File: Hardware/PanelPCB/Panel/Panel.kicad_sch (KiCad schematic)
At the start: 13 parts, among them J1 RJ45, J2 Conn_01x03_Socket, U1 AP2204R-5.0, U2 SN74LV1T34DBV

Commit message: Export schematics
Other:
- company: (none) -> M. Scholjegerdes
- title: (none) -> BugWiper 2.0 Control Panel PCB
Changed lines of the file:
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@@
 (kicad_sch (version 20230121) (generator eeschema)
   (paper "A4")
+  (title_block
+    (title "BugWiper 2.0 Control Panel PCB")
+    (date "2025-01-27")
+    (company "M. Scholjegerdes")
+  )
   (junction (at 180.34 48.26) (diameter 0) (color 0 0 0 0)
   )

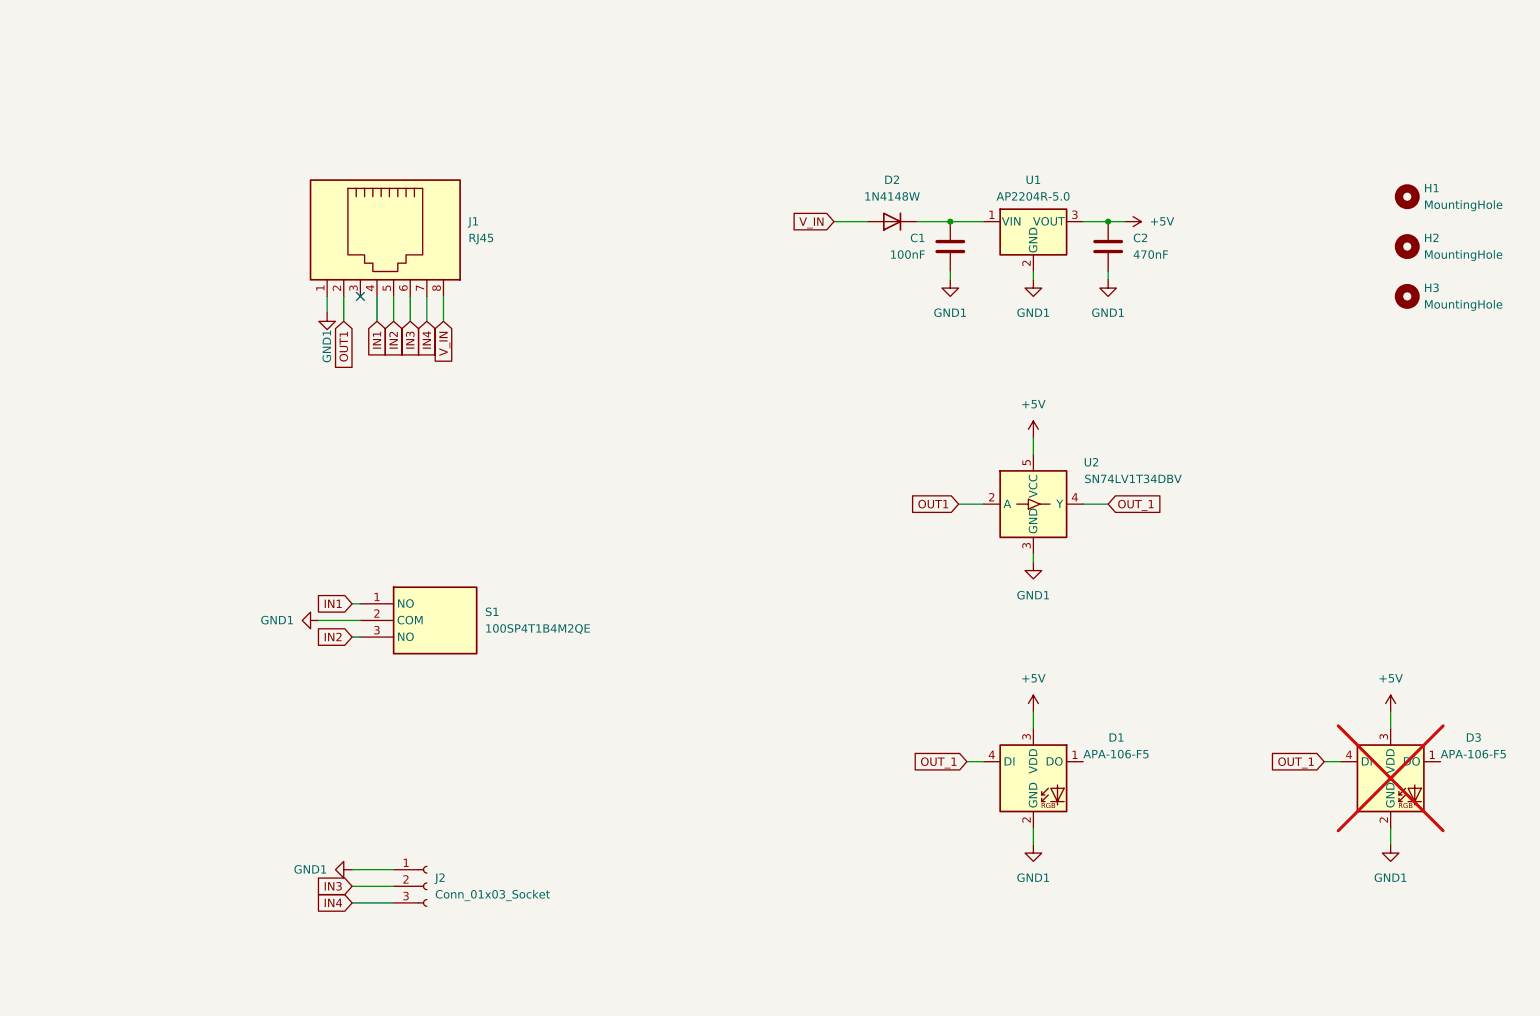
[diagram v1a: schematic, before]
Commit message: update ControlPanel PCB
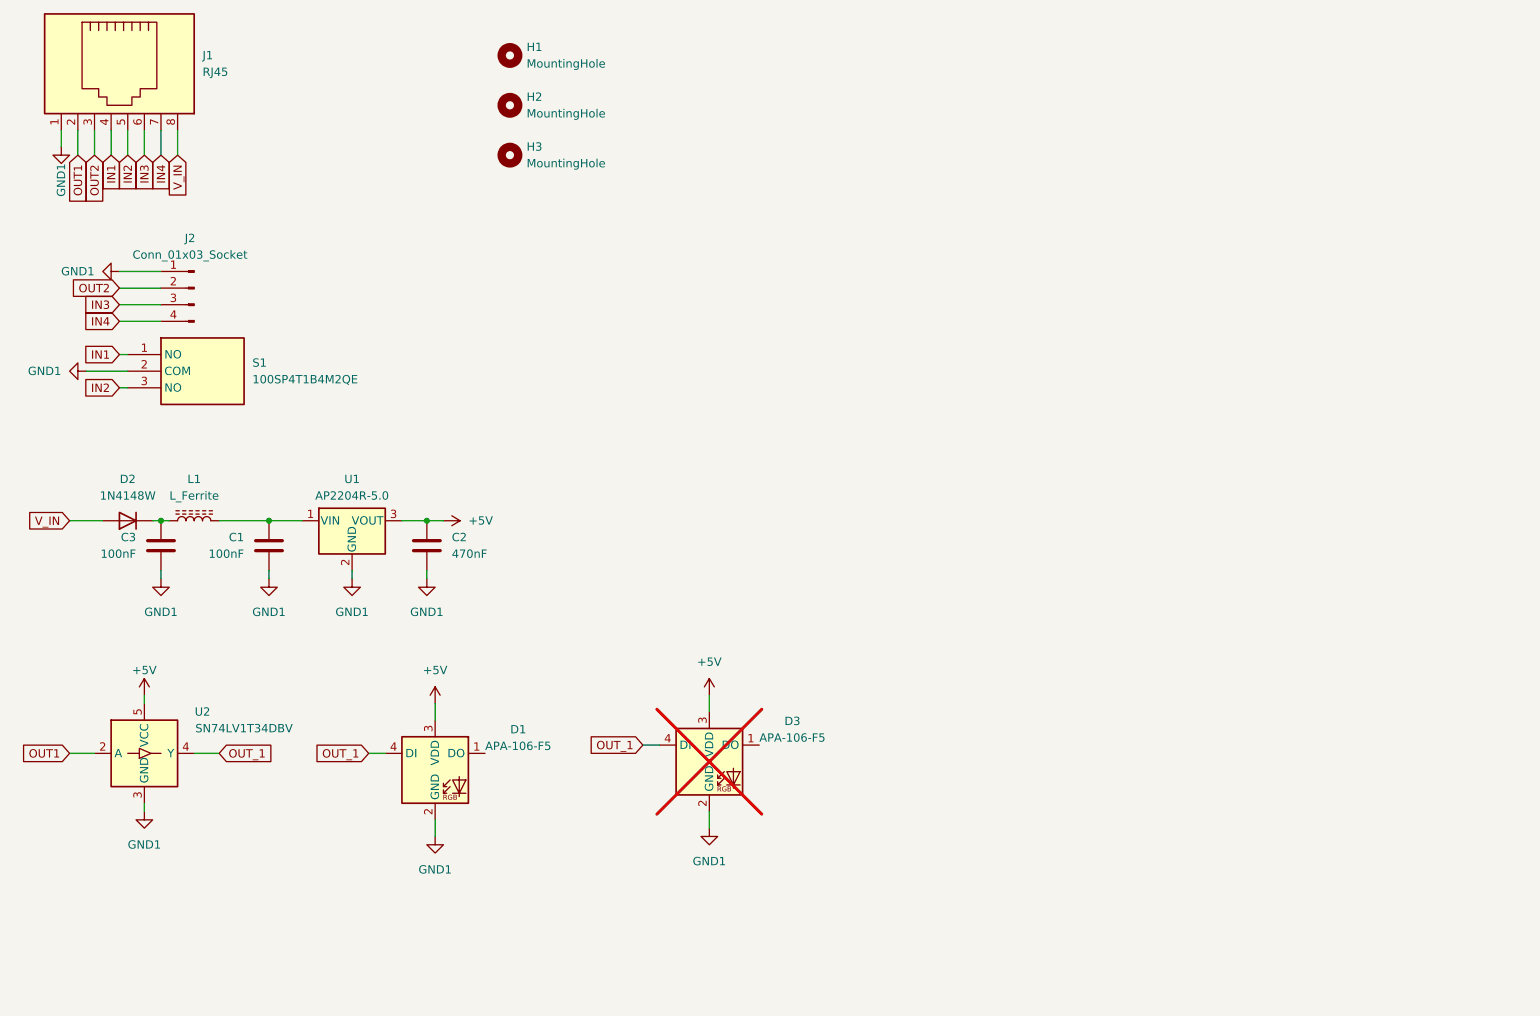
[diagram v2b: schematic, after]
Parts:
- added C3: 100nF, Capacitor_SMD:C_0603_1608Metric, symbol Device:C
- added L1: L_Ferrite, Inductor_SMD:L_0805_2012Metric, symbol Device:L_Ferrite
- J2: footprint Connector_PinHeader_2.54mm:PinHeader_1x03_P2.54mm_Vertical -> Connector_PinHeader_2.54mm:PinHeader_1x04_P2.54mm_Vertical; symbol Connector:Conn_01x03_Socket -> Connector:Conn_01x04_Pin
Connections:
- net GND1: now also C3.2
- net IN3: now also J2.3 (Pin_3); no longer J2.2 (Pin_2)
- net IN4: now also J2.4 (Pin_4); no longer J2.3 (Pin_3)
- net at C1.1, U1.1 (VIN): now also L1.2; no longer D2.1 (K)
- net OUT2: now reaches J1.3
- net OUT2: now also J2.2 (Pin_2)
- new net: C3.1, D2.1 (K), L1.1
- no-connect marks 1 -> 0
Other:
- moved on the sheet: C1, C2, D1, D2, D3, H1, H2, H3, J1, S1, U1, U2

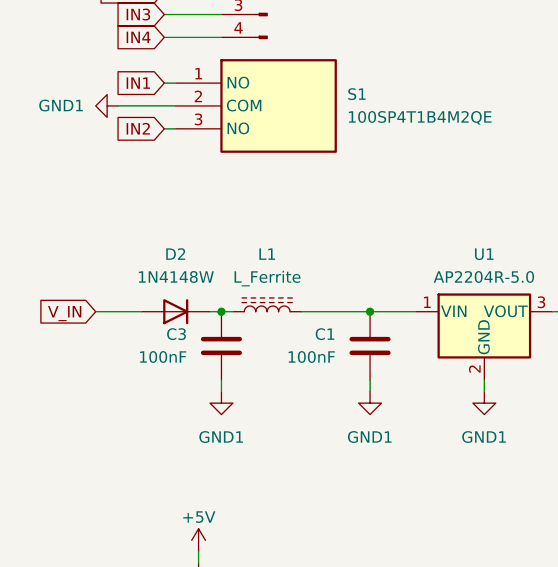
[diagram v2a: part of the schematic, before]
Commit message: update PanelPCB and generade a DualPanelPCB
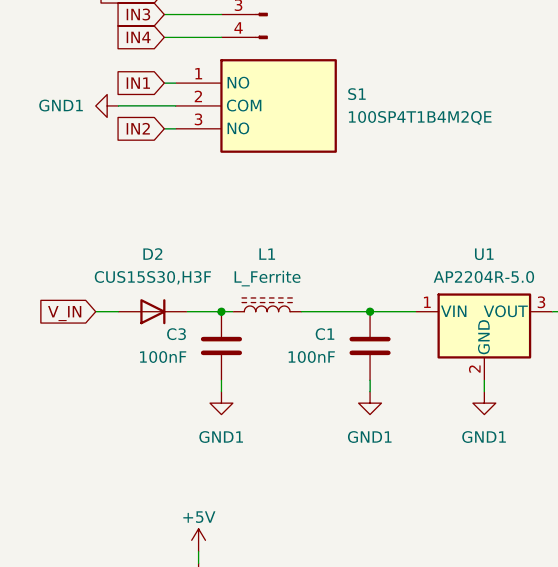
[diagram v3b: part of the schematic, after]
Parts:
- D1, D3: footprint LED_THT:LED_D5.0mm-4_RGB -> LED_THT:LED_D5.0mm-4_RGB_Wide_Pins
- D2: value 1N4148W -> CUS15S30,H3F; footprint Diode_SMD:D_SOD-123 -> Diode_SMD:D_SOD-323_HandSoldering
- H1, H2, H3: footprint MountingHole:MountingHole_2.2mm_M2_DIN965 -> MountingHole:MountingHole_2.7mm_M2.5_DIN965_Pad
- U1: Manufacturer_Name (none) -> Diodes Incorporated; Manufacturer_Part_Number (none) -> AP2204R-5.0TRG1; Packeg (none) -> SOT-89-3; Price (none) -> 1€
- U2: Manufacturer_Name (none) -> Texas Instruments; Manufacturer_Part_Number (none) -> SN74LV1T34DBVR; Mouser Part Number (none) -> 595-SN74LV1T34DBVR; Packeg (none) -> SOT-23-5; Price (none) -> 0,4€
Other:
- moved on the sheet: D2

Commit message: update BOM
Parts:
- C1, C3: Manufacturer_Name (none) -> Samsung Electro-Mechanics; Manufacturer_Part_Number (none) -> CL10B104KB8NNNC; Mouser Part Number (none) -> 187-CL10B104KB8NNNC
- C2: Manufacturer_Name (none) -> Samsung Electro-Mechanics; Manufacturer_Part_Number (none) -> CL10B474KA8NFNC; Mouser Part Number (none) -> 187-CL10B474KA8NFNC; Mouser Price/Stock (none) -> 0,038 €
- D1: Manufacturer_Name (none) -> SparkFun; Manufacturer_Part_Number (none) -> APA-106-F5
- D2: Manufacturer_Name (none) -> Toshiba; Manufacturer_Part_Number (none) -> CUS15S30,H3F; Mouser Part Number (none) -> 757-CUS15S30H3F; Mouser Price/Stock (none) -> 0,209 €
- D3: Manufacturer_Name (none) -> SparkFun; Manufacturer_Part_Number (none) -> APA-106-F5; now left out of the parts list
- H1, H2, H3: now left out of the parts list
- J1: Manufacturer_Name (none) -> GCT; Manufacturer_Part_Number (none) -> MJ3415-88-2; Mouser Part Number (none) -> 640-MJ3415-88-2; Mouser Price/Stock (none) -> 0,599 €
- J2: now not fitted; now left out of the parts list
- L1: Manufacturer_Name (none) -> Vishay / Dale; Manufacturer_Part_Number (none) -> ILBB0805ER151V; Mouser Part Number (none) -> 70-ILBB0805ER151V; Mouser Price/Stock (none) -> 0,095 €
- S1: Mouser Price/Stock https://www.mouser.com/Search/Refine.aspx?Keyword=612-100SP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 -> (none)
- U1: Mouser Part Number (none) -> 621-AP2204R-5.0TRG1; Price 1€ -> (none)
- U2: Price 0,4€ -> (none)
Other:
- moved on the sheet: C1, C2, C3, D1, D2, D3, H1, H2, H3, J1, L1, S1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
